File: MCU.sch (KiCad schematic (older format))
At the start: 10 parts, among them U2 TPS70925, U3 STM32L011F4Ux

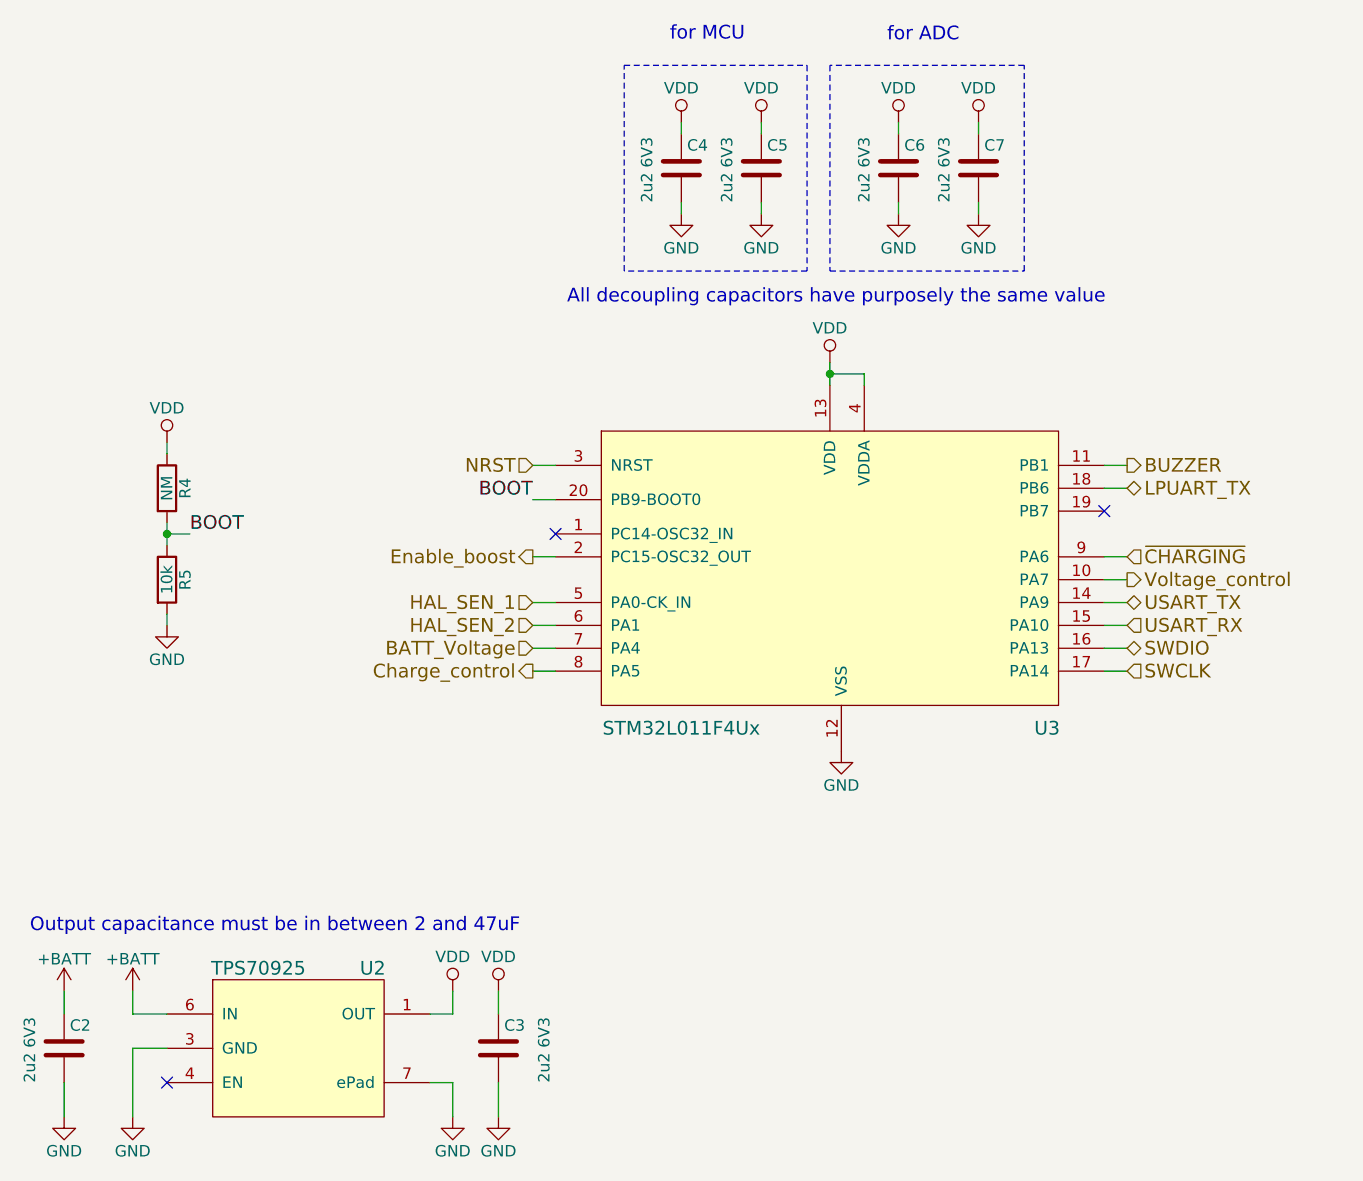
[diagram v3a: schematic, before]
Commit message: Changed pinout, added voltage and current reading
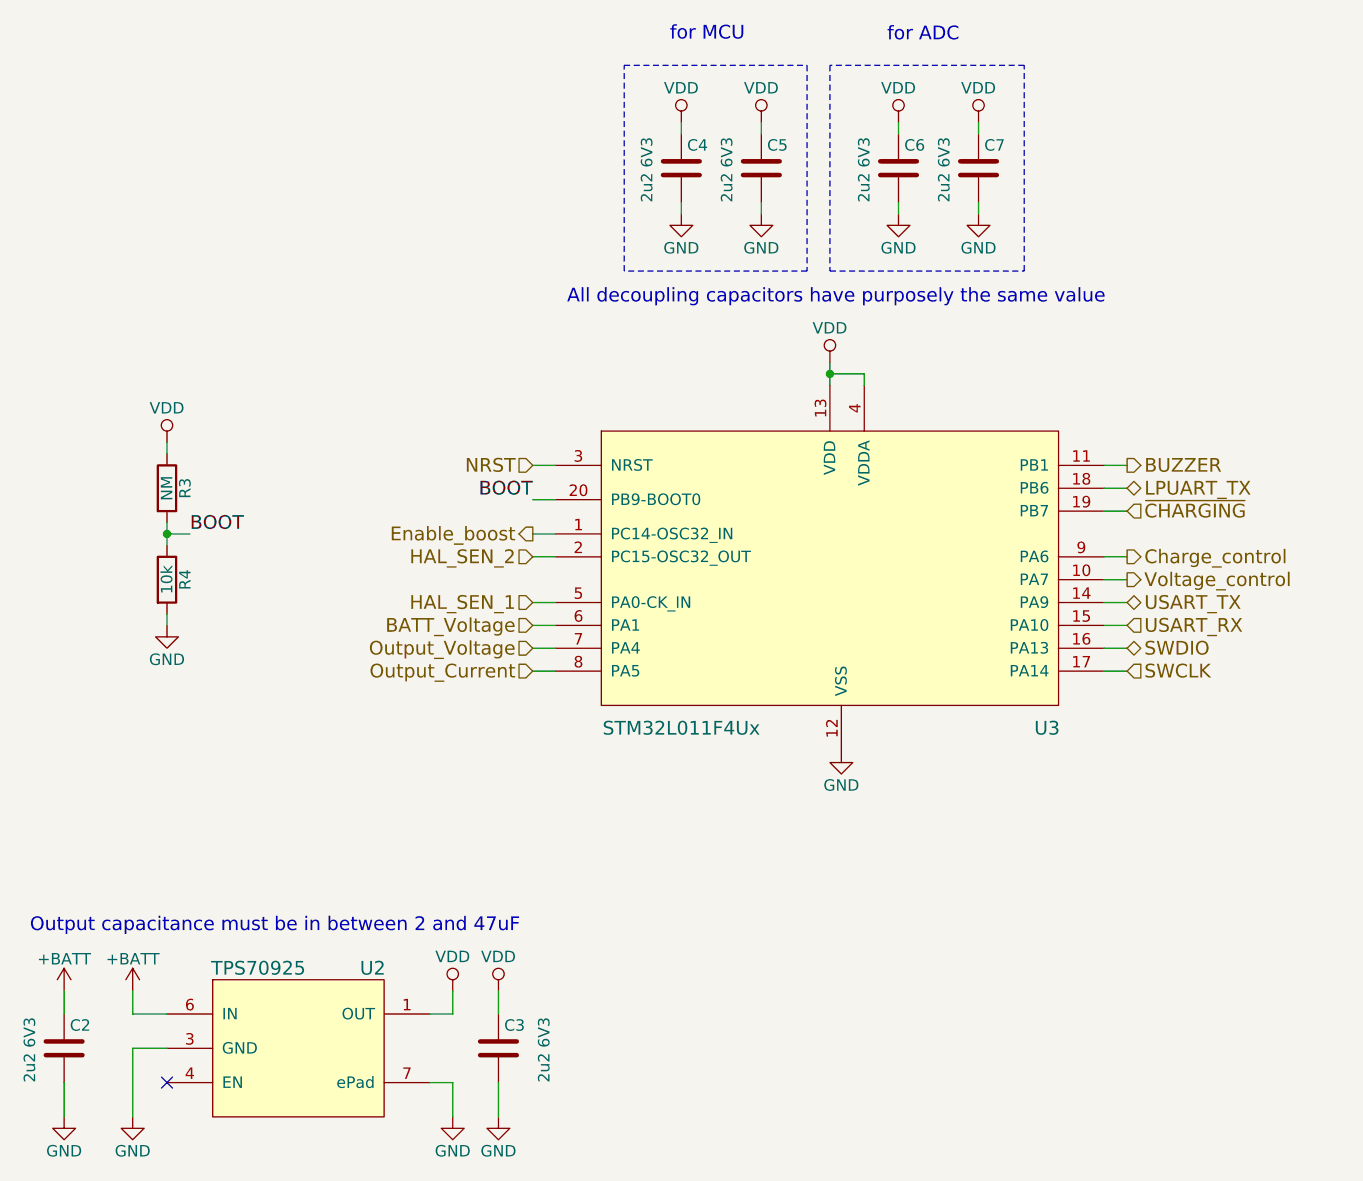
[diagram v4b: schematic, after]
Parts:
- renumbered R4 to R3, R5 to R4
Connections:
- net BATT_Voltage: now also U3.6 (PA1); no longer U3.7 (PA4)
- net Charge_control: now also U3.9 (PA6); no longer U3.8 (PA5)
- net Enable_boost: now also U3.1 (PC14-OSC32_IN); no longer U3.2 (PC15-OSC32_OUT)
- net HAL_SEN_2: now also U3.2 (PC15-OSC32_OUT); no longer U3.6 (PA1)
- net ~CHARGING: now also U3.19 (PB7); no longer U3.9 (PA6)
- new net Output_Current: U3.8 (PA5)
- new net Output_Voltage: U3.7 (PA4)
- no-connect marks 3 -> 1
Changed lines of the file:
@@
 $EndDescr
 $Comp
-L VDD #PWR012
+L VDD #PWR26
 U 1 1 5A9B30A9
 P 6100 3250
-F 0 "#PWR012" H 6100 3100 50  0001 C CNN
+F 0 "#PWR26" H 6100 3100 50  0001 C CNN
 F 1 "VDD" H 6100 3400 50  0000 C CNN
 F 2 "" H 6100 3250 50  0001 C CNN
@@
 Connection ~ 6100 3300
 $Comp
-L GND #PWR013
+L GND #PWR27
 U 1 1 5A9B30B3
 P 6150 4950
-F 0 "#PWR013" H 6150 4700 50  0001 C CNN
+F 0 "#PWR27" H 6150 4700 50  0001 C CNN
 F 1 "GND" H 6150 4800 50  0000 C CNN
 F 2 "" H 6150 4950 50  0001 C CNN
@@
 $EndComp
 $Comp
-L GND #PWR014
+L GND #PWR15
 U 1 1 5A9B3148
 P 3050 6550
-F 0 "#PWR014" H 3050 6300 50  0001 C CNN
+F 0 "#PWR15" H 3050 6300 50  0001 C CNN
 F 1 "GND" H 3050 6400 50  0000 C CNN
 F 2 "" H 3050 6550 50  0001 C CNN
@@
 NoConn ~ 3200 6400
 $Comp
-L GND #PWR015
+L GND #PWR19
 U 1 1 5A9B3188
 P 4450 6550
-F 0 "#PWR015" H 4450 6300 50  0001 C CNN
+F 0 "#PWR19" H 4450 6300 50  0001 C CNN
 F 1 "GND" H 4450 6400 50  0000 C CNN
 F 2 "" H 4450 6550 50  0001 C CNN
@@
 	4450 6400 4450 6550
 $Comp
-L VDD #PWR016
+L VDD #PWR18
 U 1 1 5A9B31B3
 P 4450 6000
-F 0 "#PWR016" H 4450 5850 50  0001 C CNN
+F 0 "#PWR18" H 4450 5850 50  0001 C CNN
 F 1 "VDD" H 4450 6150 50  0000 C CNN
 F 2 "" H 4450 6000 50  0001 C CNN
@@
 	4450 6100 4350 6100
 $Comp
-L +BATT #PWR017
+L +BATT #PWR14
 U 1 1 5A9B31F8
 P 3050 6000
-F 0 "#PWR017" H 3050 5850 50  0001 C CNN
+F 0 "#PWR14" H 3050 5850 50  0001 C CNN
 F 1 "+BATT" H 3050 6140 50  0000 C CNN
 F 2 "" H 3050 6000 50  0001 C CNN
@@
 $EndComp
 $Comp
-L VDD #PWR018
+L VDD #PWR20
 U 1 1 5A9B32A8
 P 4650 6000
-F 0 "#PWR018" H 4650 5850 50  0001 C CNN
+F 0 "#PWR20" H 4650 5850 50  0001 C CNN
 F 1 "VDD" H 4650 6150 50  0000 C CNN
 F 2 "" H 4650 6000 50  0001 C CNN
@@
 $EndComp
 $Comp
-L GND #PWR019
+L GND #PWR21
 U 1 1 5A9B32D5
 P 4650 6550
-F 0 "#PWR019" H 4650 6300 50  0001 C CNN
+F 0 "#PWR21" H 4650 6300 50  0001 C CNN
 F 1 "GND" H 4650 6400 50  0000 C CNN
 F 2 "" H 4650 6550 50  0001 C CNN
@@
 $EndComp
 $Comp
-L GND #PWR020
+L GND #PWR13
 U 1 1 5A9B33C8
 P 2750 6550
-F 0 "#PWR020" H 2750 6300 50  0001 C CNN
+F 0 "#PWR13" H 2750 6300 50  0001 C CNN
 F 1 "GND" H 2750 6400 50  0000 C CNN
 F 2 "" H 2750 6550 50  0001 C CNN
@@
 	2750 6400 2750 6550
 $Comp
-L +BATT #PWR021
+L +BATT #PWR12
 U 1 1 5A9B33E9
 P 2750 6000
-F 0 "#PWR021" H 2750 5850 50  0001 C CNN
+F 0 "#PWR12" H 2750 5850 50  0001 C CNN
 F 1 "+BATT" H 2750 6140 50  0000 C CNN
 F 2 "" H 2750 6000 50  0001 C CNN
@@
 Output capacitance must be in between 2 and 47uF\n
 $Comp
-L VDD #PWR022
+L VDD #PWR22
 U 1 1 5A9B3944
 P 5450 2200
-F 0 "#PWR022" H 5450 2050 50  0001 C CNN
+F 0 "#PWR22" H 5450 2050 50  0001 C CNN
 F 1 "VDD" H 5450 2350 50  0000 C CNN
 F 2 "" H 5450 2200 50  0001 C CNN
@@
 	5450 2200 5450 2250
 $Comp
-L GND #PWR023
+L GND #PWR23
 U 1 1 5A9B3984
 P 5450 2600
-F 0 "#PWR023" H 5450 2350 50  0001 C CNN
+F 0 "#PWR23" H 5450 2350 50  0001 C CNN
 F 1 "GND" H 5450 2450 50  0000 C CNN
 F 2 "" H 5450 2600 50  0001 C CNN
@@
 $EndComp
 $Comp
-L VDD #PWR024
+L VDD #PWR24
 U 1 1 5A9B39F3
 P 5800 2200
-F 0 "#PWR024" H 5800 2050 50  0001 C CNN
+F 0 "#PWR24" H 5800 2050 50  0001 C CNN
 F 1 "VDD" H 5800 2350 50  0000 C CNN
 F 2 "" H 5800 2200 50  0001 C CNN
@@
 	5800 2200 5800 2250
 $Comp
-L GND #PWR025
+L GND #PWR25
 U 1 1 5A9B39FA
 P 5800 2600
-F 0 "#PWR025" H 5800 2350 50  0001 C CNN
+F 0 "#PWR25" H 5800 2350 50  0001 C CNN
 F 1 "GND" H 5800 2450 50  0000 C CNN
 F 2 "" H 5800 2600 50  0001 C CNN
@@
 $EndComp
 $Comp
-L VDD #PWR026
+L VDD #PWR28
 U 1 1 5A9B3B2B
 P 6400 2200
-F 0 "#PWR026" H 6400 2050 50  0001 C CNN
+F 0 "#PWR28" H 6400 2050 50  0001 C CNN
 F 1 "VDD" H 6400 2350 50  0000 C CNN
 F 2 "" H 6400 2200 50  0001 C CNN
@@
 	6400 2200 6400 2250
 $Comp
-L GND #PWR027
+L GND #PWR29
 U 1 1 5A9B3B32
 P 6400 2600
-F 0 "#PWR027" H 6400 2350 50  0001 C CNN
+F 0 "#PWR29" H 6400 2350 50  0001 C CNN
 F 1 "GND" H 6400 2450 50  0000 C CNN
 F 2 "" H 6400 2600 50  0001 C CNN
@@
 $EndComp
 $Comp
-L VDD #PWR028
+L VDD #PWR30
 U 1 1 5A9B3B8A
 P 6750 2200
-F 0 "#PWR028" H 6750 2050 50  0001 C CNN
+F 0 "#PWR30" H 6750 2050 50  0001 C CNN
 F 1 "VDD" H 6750 2350 50  0000 C CNN
 F 2 "" H 6750 2200 50  0001 C CNN
@@
 	6750 2200 6750 2250
 $Comp
-L GND #PWR029
+L GND #PWR31
 U 1 1 5A9B3B91
 P 6750 2600
-F 0 "#PWR029" H 6750 2350 50  0001 C CNN
+F 0 "#PWR31" H 6750 2350 50  0001 C CNN
 F 1 "GND" H 6750 2450 50  0000 C CNN
 F 2 "" H 6750 2600 50  0001 C CNN
@@
 	7300 4500 7400 4500
 $Comp
-L R R5
+L R R4
 U 1 1 5A9B431F
 P 3200 4200
-F 0 "R5" V 3280 4200 50  0000 C CNN
+F 0 "R4" V 3280 4200 50  0000 C CNN
 F 1 "10k" V 3200 4200 50  0000 C CNN
 F 2 "Resistors_SMD:R_0402" V 3130 4200 50  0001 C CNN
@@
 $EndComp
 $Comp
-L R R4
+L R R3
 U 1 1 5A9B4434
 P 3200 3800
-F 0 "R4" V 3280 3800 50  0000 C CNN
+F 0 "R3" V 3280 3800 50  0000 C CNN
 F 1 "NM" V 3200 3800 50  0000 C CNN
 F 2 "Resistors_SMD:R_0402" V 3130 3800 50  0001 C CNN
@@
 $EndComp
 $Comp
-L VDD #PWR030
+L VDD #PWR16
 U 1 1 5A9B4476
 P 3200 3600
-F 0 "#PWR030" H 3200 3450 50  0001 C CNN
+F 0 "#PWR16" H 3200 3450 50  0001 C CNN
 F 1 "VDD" H 3200 3750 50  0000 C CNN
 F 2 "" H 3200 3600 50  0001 C CNN
@@
 	3200 3650 3200 3600
 $Comp
-L GND #PWR031
+L GND #PWR17
 U 1 1 5A9B4528
 P 3200 4400
-F 0 "#PWR031" H 3200 4150 50  0001 C CNN
+F 0 "#PWR17" H 3200 4150 50  0001 C CNN
 F 1 "GND" H 3200 4250 50  0000 C CNN
 F 2 "" H 3200 4400 50  0001 C CNN
@@
 Wire Wire Line
 	4800 4300 4900 4300
-Text HLabel 4800 4400 0    60   Input ~ 0
+Text HLabel 4800 4100 0    60   Input ~ 0
 HAL_SEN_2
 Text HLabel 7400 3700 2    60   Output ~ 0
@@
 Text HLabel 7400 4200 2    60   Output ~ 0
 Voltage_control
-Text HLabel 4800 4100 0    60   Output ~ 0
+Text HLabel 4800 4000 0    60   Output ~ 0
 Enable_boost
 Wire Wire Line
-	4800 4500 4900 4500
-Text HLabel 4800 4500 0    60   Input ~ 0
+	4800 4400 4900 4400
+Text HLabel 4800 4400 0    60   Input ~ 0
 BATT_Voltage
 Wire Wire Line
 	7300 3700 7400 3700
 Wire Wire Line
-	4800 4600 4900 4600
-Wire Wire Line
-	4800 4100 4900 4100
+	7300 4100 7400 4100
+Wire Wire Line
+	4800 4000 4900 4000
 $Comp
 L TPS709 U2
@@
 Text Notes 4950 3000 0    60   ~ 0
 All decoupling capacitors have purposely the same value\n
-Text HLabel 7400 4100 2    60   Input ~ 0
+Text HLabel 7400 3900 2    60   Input ~ 0
 ~CHARGING
-Text HLabel 4800 4600 0    60   Output ~ 0
+Text HLabel 7400 4100 2    60   Output ~ 0
 Charge_control
 Wire Wire Line
 	7300 4200 7400 4200
 Wire Wire Line
-	4900 4400 4800 4400
-Wire Wire Line
-	7400 4100 7300 4100
+	4900 4100 4800 4100
+Wire Wire Line
+	7400 3900 7300 3900
 Text HLabel 7400 3800 2    60   BiDi ~ 0
 LPUART_TX
 Wire Wire Line
 	7300 3800 7400 3800
-NoConn ~ 7300 3900
 $Comp
 L STM32L011F4Ux U3
@@
 	1    0    0    -1
 $EndComp
-NoConn ~ 4900 4000
+Text HLabel 4800 4500 0    60   Input ~ 0
+Output_Voltage
+Text HLabel 4800 4600 0    60   Input ~ 0
+Output_Current
+Wire Wire Line
+	4800 4600 4900 4600
+Wire Wire Line
+	4800 4500 4900 4500
 $EndSCHEMATC
